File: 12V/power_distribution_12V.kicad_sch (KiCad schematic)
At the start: 34 parts, among them J1 39301020, J10 39301020, J11 39301020, J2 768250004, J20 1720650004, J3 39301020, J4 768250004, J6 39301020, J7 39301020, J9 39301020, U1 RASPBERRY_PCB

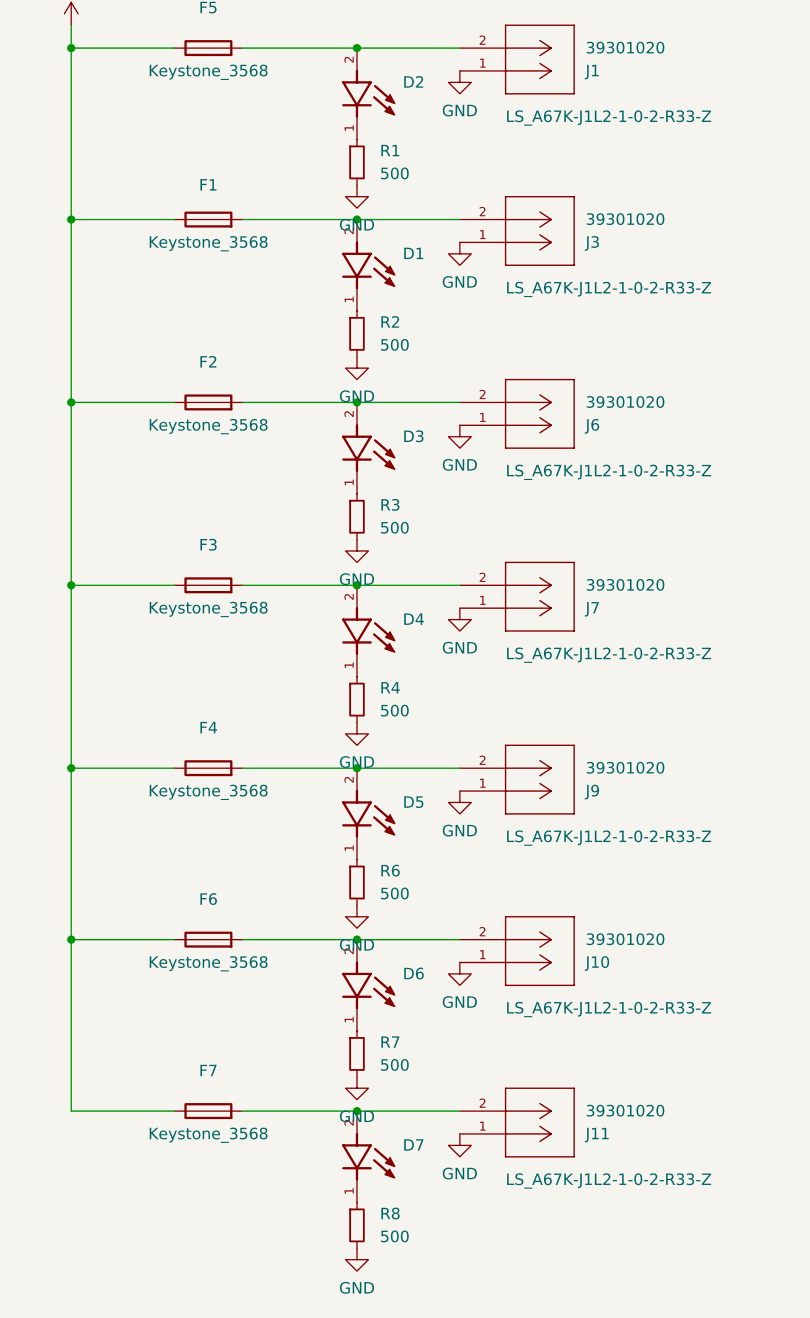
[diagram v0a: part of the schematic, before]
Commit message: corrected resistors for LEDs
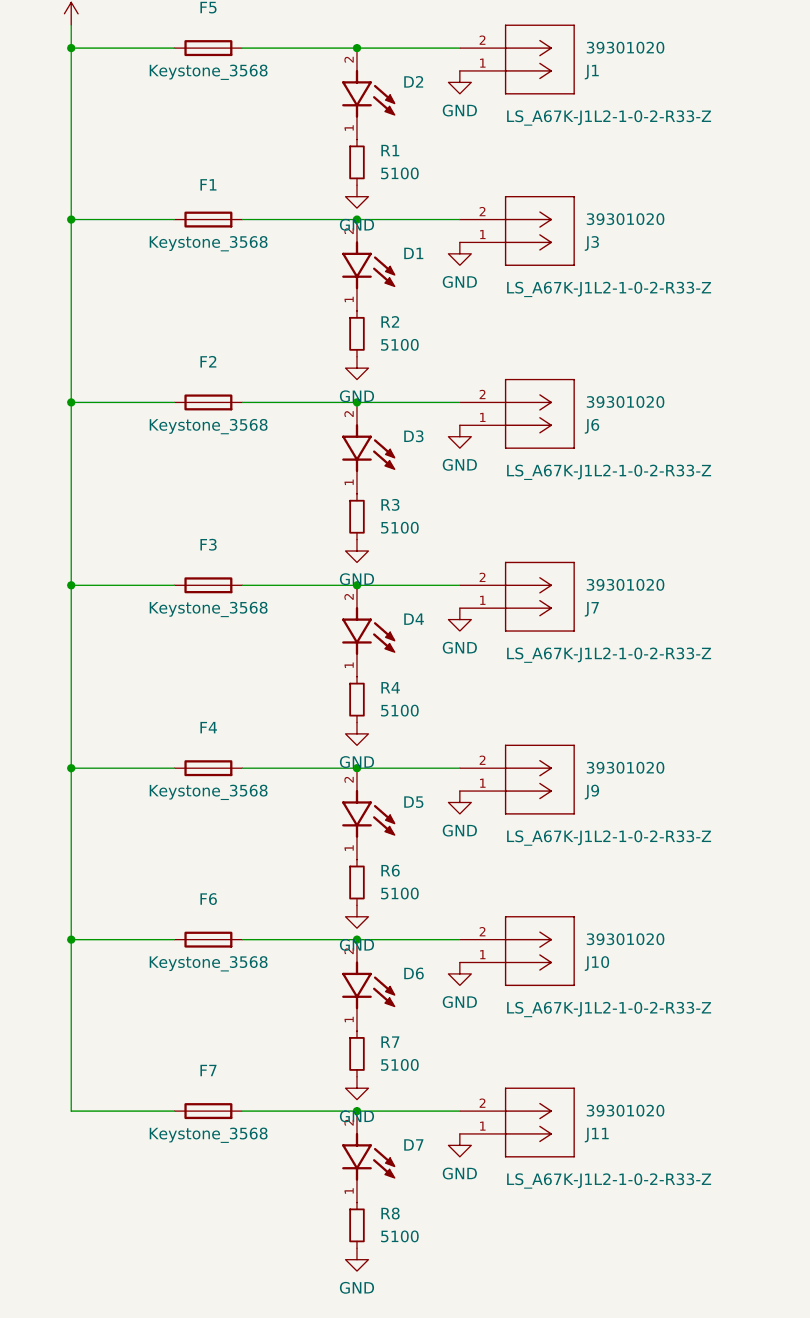
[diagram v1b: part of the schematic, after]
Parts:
- R1, R2, R3, R4, R6, R7, R8: value 500 -> 5100
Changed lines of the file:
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@@
       (effects (font (size 1.27 1.27)) (justify left))
     )
-    (property "Value" "500" (at 237.49 54.61 0)
+    (property "Value" "5100" (at 237.49 54.61 0)
       (effects (font (size 1.27 1.27)) (justify left))
     )
@@
       (effects (font (size 1.27 1.27)) (justify left))
     )
-    (property "Value" "500" (at 237.49 153.67 0)
+    (property "Value" "5100" (at 237.49 153.67 0)
       (effects (font (size 1.27 1.27)) (justify left))
     )
@@
       (effects (font (size 1.27 1.27)) (justify left))
     )
-    (property "Value" "500" (at 237.49 95.25 0)
+    (property "Value" "5100" (at 237.49 95.25 0)
       (effects (font (size 1.27 1.27)) (justify left))
     )
@@
       (effects (font (size 1.27 1.27)) (justify left))
     )
-    (property "Value" "500" (at 237.49 35.56 0)
+    (property "Value" "5100" (at 237.49 35.56 0)
       (effects (font (size 1.27 1.27)) (justify left))
     )
@@
       (effects (font (size 1.27 1.27)) (justify left))
     )
-    (property "Value" "500" (at 237.49 74.93 0)
+    (property "Value" "5100" (at 237.49 74.93 0)
       (effects (font (size 1.27 1.27)) (justify left))
     )
@@
       (effects (font (size 1.27 1.27)) (justify left))
     )
-    (property "Value" "500" (at 237.49 134.62 0)
+    (property "Value" "5100" (at 237.49 134.62 0)
       (effects (font (size 1.27 1.27)) (justify left))
     )
@@
       (effects (font (size 1.27 1.27)) (justify left))
     )
-    (property "Value" "500" (at 237.49 115.57 0)
-      (effects (font (size 1.27 1.27)) (justify left))
-    )
+    (property "Value" "5100" (at 237.49 115.57 0)
+      (effects (font (size 1.27 1.27)) (justify left))
+    )

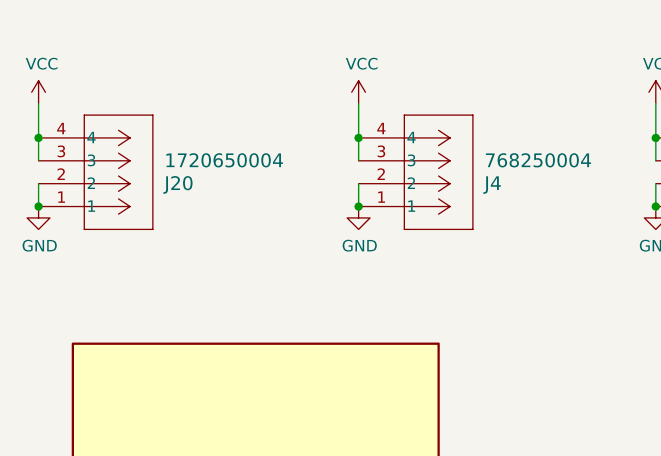
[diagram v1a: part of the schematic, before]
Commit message: added 3d models to the pcbs
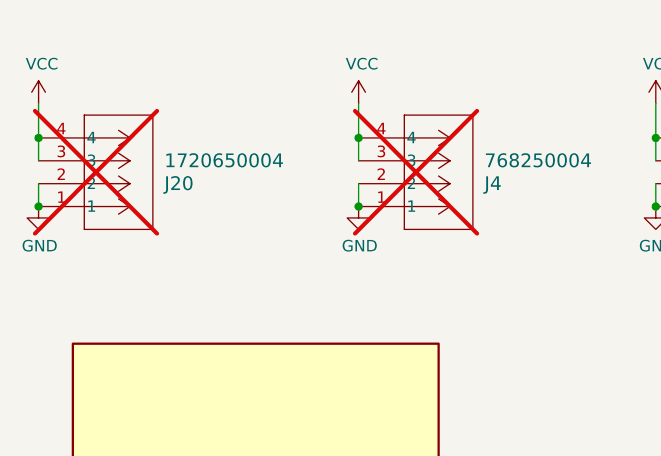
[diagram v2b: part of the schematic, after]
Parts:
- J20, J4: now not fitted
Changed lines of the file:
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@@
   )
   (symbol (lib_id "mega_fit_stehend:1720650004") (at 26.67 34.29 0) (mirror x) (unit 1)
-    (in_bom yes) (on_board yes) (dnp no)
+    (in_bom yes) (on_board yes) (dnp yes)
     (property "Reference" "J20" (at 40.64 31.75 0)
       (effects (font (size 1.524 1.524)) (justify left))
@@
   )
   (symbol (lib_id "mega_fit:768250004") (at 62.23 34.29 0) (mirror x) (unit 1)
-    (in_bom yes) (on_board yes) (dnp no)
+    (in_bom yes) (on_board yes) (dnp yes)
     (property "Reference" "J4" (at 76.2 31.75 0)
       (effects (font (size 1.524 1.524)) (justify left))
